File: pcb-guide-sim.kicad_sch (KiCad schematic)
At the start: 2 parts

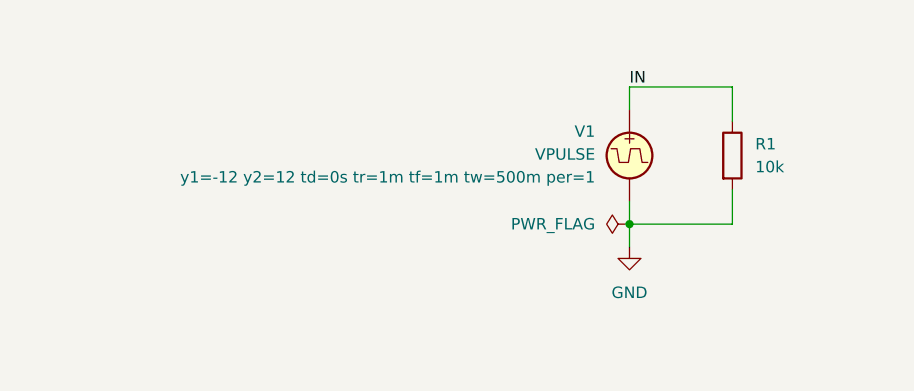
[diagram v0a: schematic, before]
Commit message: Add PMOS transistor
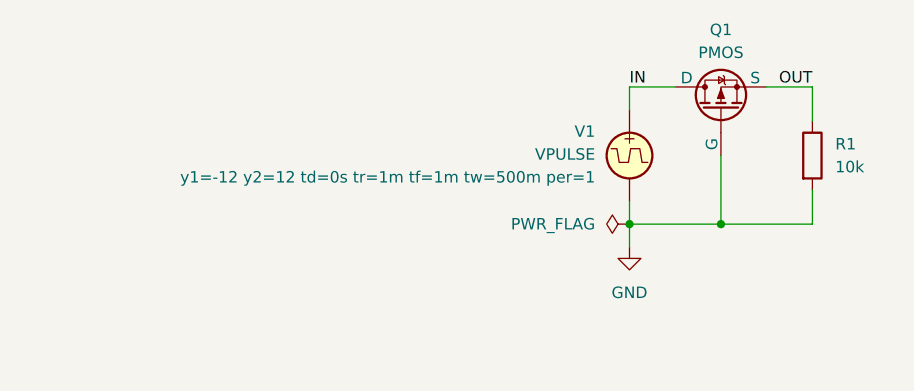
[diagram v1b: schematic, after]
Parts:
- added Q1: PMOS, symbol Simulation_SPICE:PMOS
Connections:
- net GND: now also Q1.2 (G)
- net IN: now also Q1.1 (D); no longer R1.1
- new net OUT: Q1.3 (S), R1.1
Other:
- moved on the sheet: R1
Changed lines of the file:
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@@
 		(color 0 0 0 0)
 	)
+	(junction
+		(at 152.4 111.76)
+		(diameter 0)
+		(color 0 0 0 0)
+	)
+	(wire
+		(pts
+			(xy 142.24 96.52) (xy 147.32 96.52)
+		)
+		(stroke
+			(width 0)
+			(type default)
+		)
+	)
 	(wire
 		(pts
@@
 	(wire
 		(pts
-			(xy 142.24 96.52) (xy 153.67 96.52)
-		)
-		(stroke
-			(width 0)
-			(type default)
-		)
-	)
-	(wire
-		(pts
-			(xy 142.24 111.76) (xy 153.67 111.76)
-		)
-		(stroke
-			(width 0)
-			(type default)
-		)
-	)
-	(wire
-		(pts
-			(xy 153.67 96.52) (xy 153.67 100.33)
-		)
-		(stroke
-			(width 0)
-			(type default)
-		)
-	)
-	(wire
-		(pts
-			(xy 153.67 111.76) (xy 153.67 107.95)
+			(xy 142.24 111.76) (xy 152.4 111.76)
+		)
+		(stroke
+			(width 0)
+			(type default)
+		)
+	)
+	(wire
+		(pts
+			(xy 162.56 96.52) (xy 162.56 100.33)
+		)
+		(stroke
+			(width 0)
+			(type default)
+		)
+	)
+	(wire
+		(pts
+			(xy 162.56 111.76) (xy 162.56 107.95)
+		)
+		(stroke
+			(width 0)
+			(type default)
+		)
+	)
+	(wire
+		(pts
+			(xy 152.4 104.14) (xy 152.4 111.76)
+		)
+		(stroke
+			(width 0)
+			(type default)
+		)
+	)
+	(wire
+		(pts
+			(xy 152.4 111.76) (xy 162.56 111.76)
 		)
 		(stroke
@@
 		(pts
 			(xy 142.24 99.06) (xy 142.24 96.52)
+		)
+		(stroke
+			(width 0)
+			(type default)
+		)
+	)
+	(wire
+		(pts
+			(xy 157.48 96.52) (xy 162.56 96.52)
 		)
 		(stroke
@@
 		)
 	)
+	(label "OUT"
+		(at 162.56 96.52 180)
+		(effects
+			(font
+				(size 1.27 1.27)
+			)
+			(justify right bottom)
+		)
+	)
+	(symbol
+		(lib_id "Simulation_SPICE:PMOS")
+		(at 152.4 99.06 90)
+		(unit 1)
+		(body_style 1)
+		(exclude_from_sim no)
+		(in_bom yes)
+		(on_board yes)
+		(in_pos_files yes)
+		(dnp no)
+		(fields_autoplaced yes)
+		(property "Reference" "Q1"
+			(at 152.4 90.17 90)
+			(show_name no)
+			(do_not_autoplace no)
+			(effects
+				(font
+					(size 1.27 1.27)
+				)
+			)
+		)
+		(property "Value" "PMOS"
+			(at 152.4 92.71 90)
+			(show_name no)
+			(do_not_autoplace no)
+			(effects
+				(font
+					(size 1.27 1.27)
+				)
+			)
+		)
+		(property "Footprint" ""
+			(at 149.86 93.98 0)
+			(hide yes)
+			(show_name no)
+			(do_not_autoplace no)
+			(effects
+				(font
+					(size 1.27 1.27)
+				)
+			)
+		)
+		(property "Datasheet" "https://ngspice.sourceforge.io/docs/ngspice-html-manual/manual.xhtml#cha_MOSFETs"
+			(at 165.1 99.06 0)
+			(hide yes)
+			(show_name no)
+			(do_not_autoplace no)
+			(effects
+				(font
+					(size 1.27 1.27)
+				)
+			)
+		)
+		(property "Description" "P-MOSFET transistor, drain/source/gate"
+			(at 152.4 99.06 0)
+			(hide yes)
+			(show_name no)
+			(do_not_autoplace no)
+			(effects
+				(font
+					(size 1.27 1.27)
+				)
+			)
+		)
+		(property "Sim.Device" "PMOS"
+			(at 169.545 99.06 0)
+			(hide yes)
+			(show_name no)
+			(do_not_autoplace no)
+			(effects
+				(font
+					(size 1.27 1.27)
+				)
+			)
+		)
+		(property "Sim.Type" "VDMOS"
+			(at 171.45 99.06 0)
+			(hide yes)
+			(show_name no)
+			(do_not_autoplace no)
+			(effects
+				(font
+					(size 1.27 1.27)
+				)
+			)
+		)
+		(property "Sim.Pins" "1=D 2=G 3=S"
+			(at 167.64 99.06 0)
+			(hide yes)
+			(show_name no)
+			(do_not_autoplace no)
+			(effects
+				(font
+					(size 1.27 1.27)
+				)
+			)
+		)
+		(pin "3"
+		)
+		(pin "1"
+		)
+		(pin "2"
+		)
+		(instances
+			(project "pcb-guide-sim"
+				(path "/0124ff61-c55b-4890-8235-20d72f374281"
+					(reference "Q1")
+					(unit 1)
+				)
+			)
+		)
+	)
 	(symbol
 		(lib_id "Device:R")
-		(at 153.67 104.14 0)
+		(at 162.56 104.14 0)
 		(unit 1)
 		(body_style 1)
@@
 		(fields_autoplaced yes)
 		(property "Reference" "R1"
-			(at 156.21 102.8699 0)
+			(at 165.1 102.8699 0)
 			(show_name no)
 			(do_not_autoplace no)
@@
 		)
 		(property "Value" "10k"
-			(at 156.21 105.4099 0)
+			(at 165.1 105.4099 0)
 			(show_name no)
 			(do_not_autoplace no)
@@
 		)
 		(property "Footprint" ""
-			(at 151.892 104.14 90)
+			(at 160.782 104.14 90)
 			(hide yes)
 			(show_name no)
@@
 		)
 		(property "Datasheet" ""
-			(at 153.67 104.14 0)
+			(at 162.56 104.14 0)
 			(hide yes)
 			(show_name no)
@@
 		)
 		(property "Description" "Resistor"
-			(at 153.67 104.14 0)
-			(hide yes)
-			(show_name no)
+			(at 162.56 104.14 0)
+			(hide yes)
+			(show_name no)

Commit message: Limit GS voltage with a Zener diode
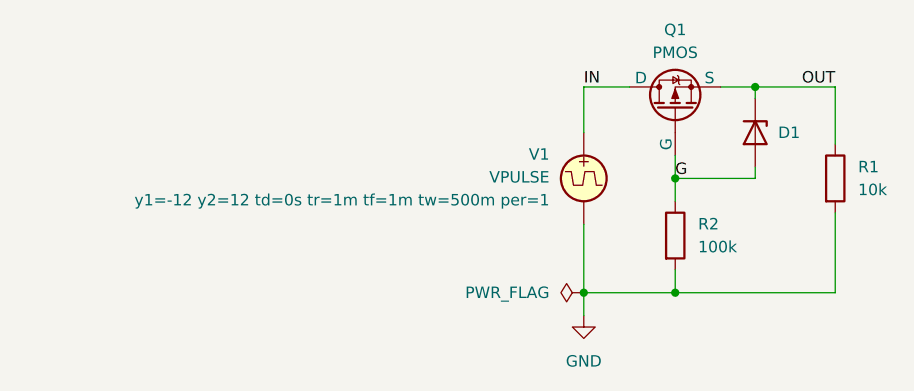
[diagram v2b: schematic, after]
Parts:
- added D1: Zener, symbol Device:D_Zener
- added R2: 100k, symbol Device:R
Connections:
- net GND: now also R2.2; no longer Q1.2 (G)
- net OUT: now also D1.1 (K)
- new net G: D1.2 (A), Q1.2 (G), R2.1
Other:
- moved on the sheet: Q1, R1, V1
